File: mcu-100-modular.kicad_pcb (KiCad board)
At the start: 2 copper layers, 0 parts

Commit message: feat(mcu-100): actualizar esquematico, pcb y configuracion modular de espadines
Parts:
- added J1: Espadines_2x15_Macho, LUISMATERIALES:PinHeader_2x15_P2.54mm_Vertical, F.Cu at (140.6, 61.7)
- added J2: Espadines_2x15_Macho, LUISMATERIALES:PinHeader_2x15_P2.54mm_Vertical, F.Cu at (95.4, 57.0)
- added J3: Espadines_2x15_Macho, LUISMATERIALES:PinHeader_2x15_P2.54mm_Vertical, F.Cu at (131.5, 102.1)
- added J4: Espadines_2x15_Macho, LUISMATERIALES:PinHeader_2x15_P2.54mm_Vertical, F.Cu at (80.8, 61.8)
- added M1: Module-mcu-0.7, hellen-one-mcu-0.7:mcu, F.Cu at (88.8, 98.0)
- added M2: Module-mega-mcu144-0.7, hellen-one-mega-mcu144-0.7:mega-mcu144, F.Cu at (19.1, 73.7)
- added M4: Module:mega-mcu100/0.3, hellen-one-mega-mcu100-0.3:mega-mcu100, F.Cu at (36.3, 121.5)
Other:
- board outline added: 229.8 x 110 mm

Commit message: fix(bom): remover modulos extra M2 y M4 para eliminar duplicados de U105 en BOM
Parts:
- removed M2: Module-mega-mcu144-0.7, hellen-one-mega-mcu144-0.7:mega-mcu144
- removed M4: Module:mega-mcu100/0.3, hellen-one-mega-mcu100-0.3:mega-mcu100

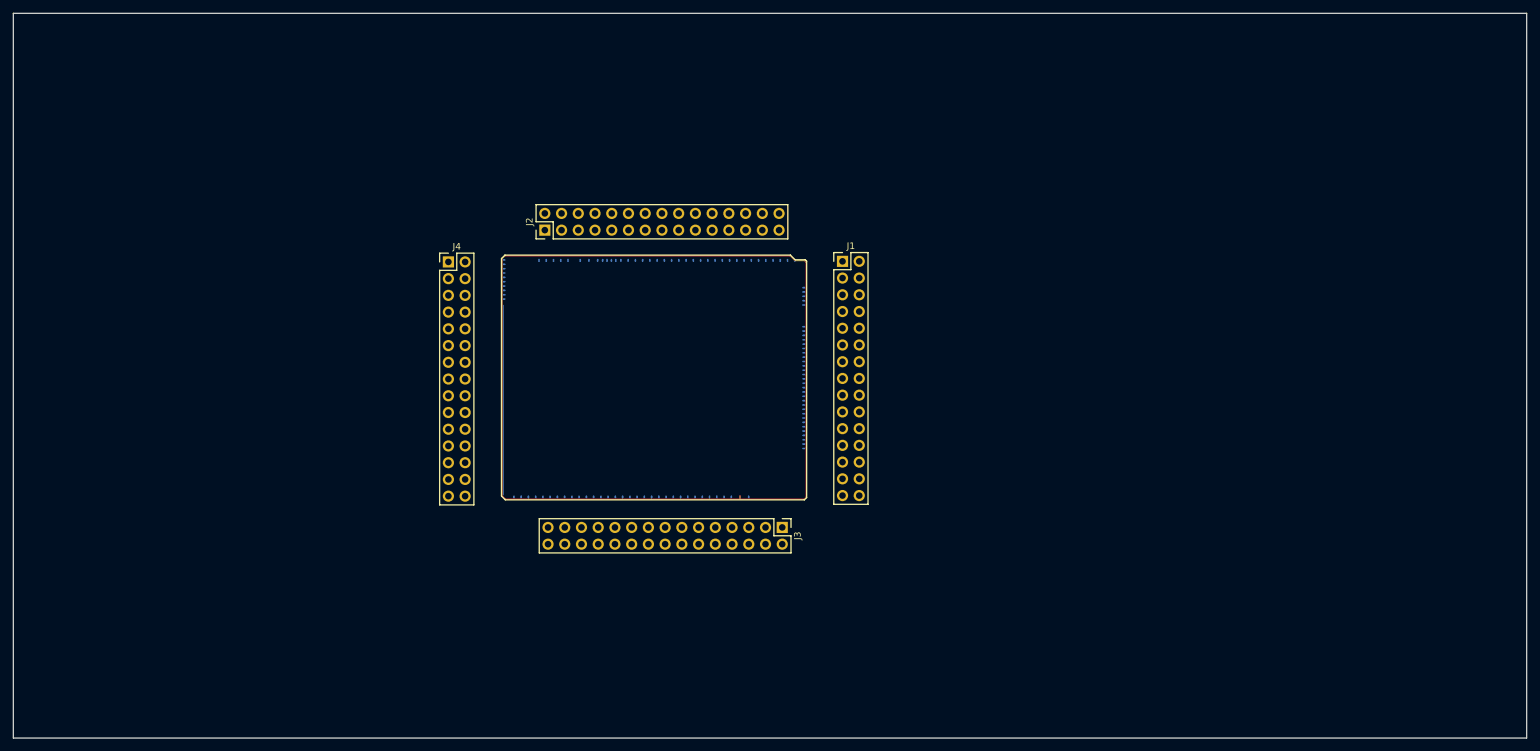
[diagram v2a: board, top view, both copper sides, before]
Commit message: feat(pcb, bom): actualizar sincronizacion PCB y anadir reemplazo U103 por AP2331SA-7 (C500764)
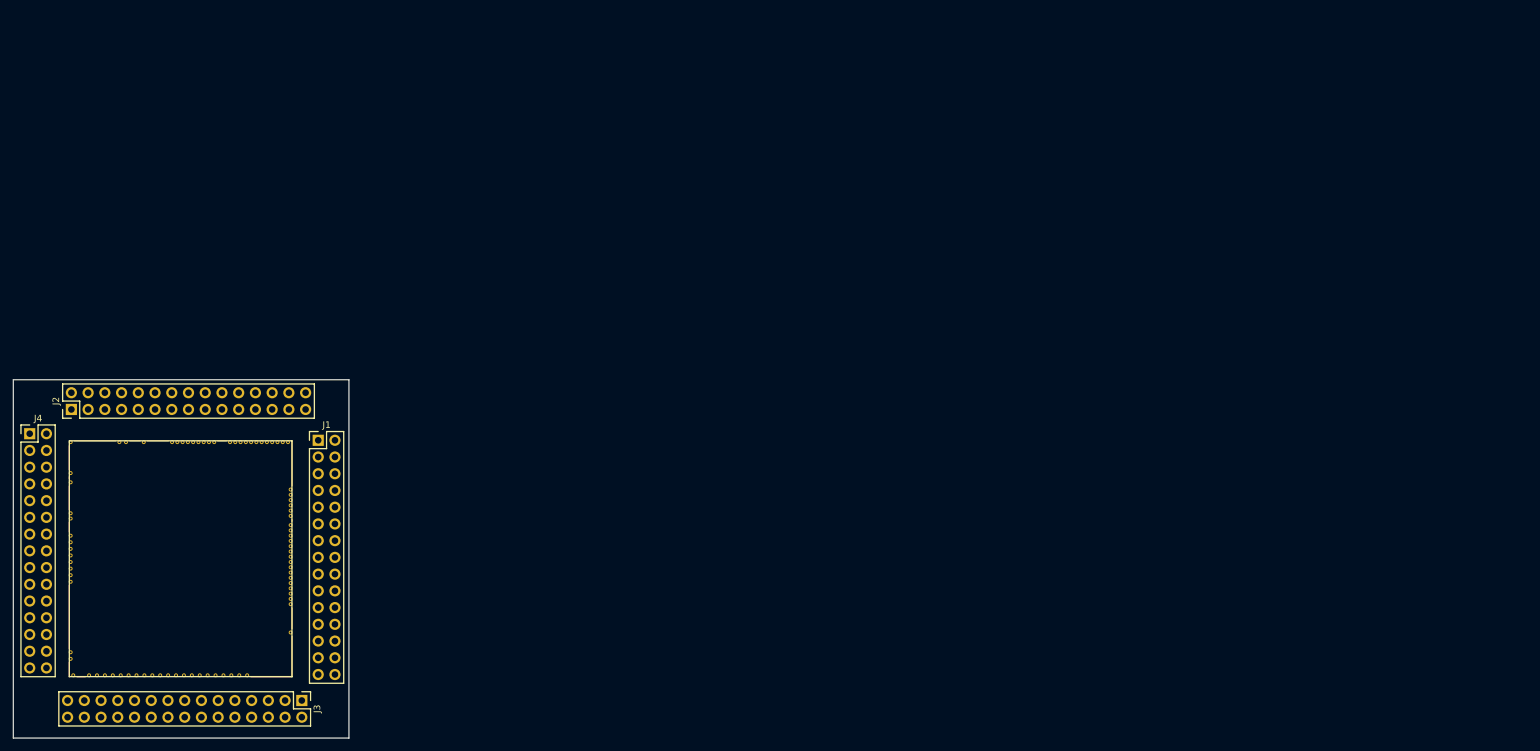
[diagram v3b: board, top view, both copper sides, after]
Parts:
- M1: value Module-mcu-0.7 -> Module:mega-mcu100/0.3; footprint hellen-one-mcu-0.7:mcu -> hellen-one-mega-mcu100-0.3:mega-mcu100
- moved J1 84.1 mm to (61.0, 88.9)
- moved J3 77.5 mm to (58.5, 128.4)
- moved J2 76.9 mm to (23.6, 84.2)
- moved M1 70.9 mm to (23.1, 124.9)
- moved J4 68.7 mm to (17.2, 87.9)
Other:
- board size 229.8 x 110 mm -> 51 x 54.4 mm

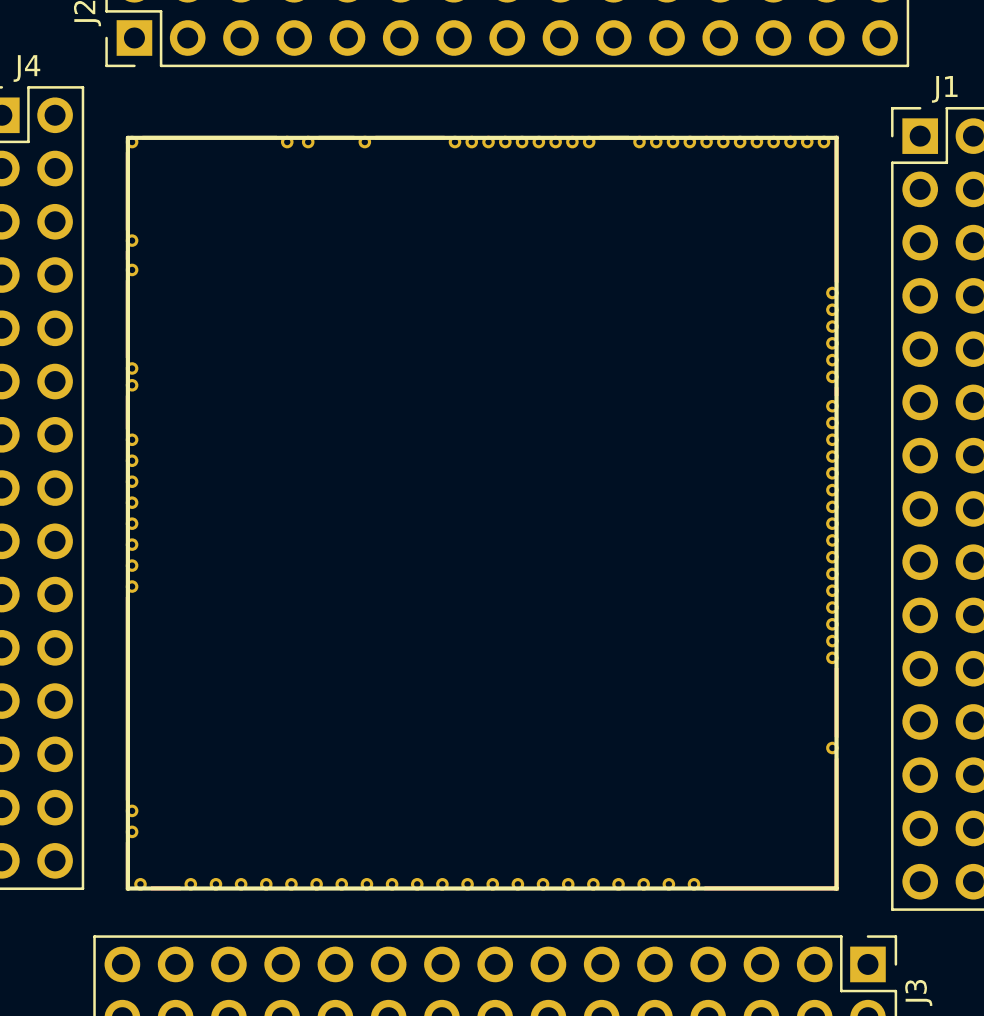
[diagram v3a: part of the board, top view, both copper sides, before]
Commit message: feat(sch, pcb): actualizar modulo M1 a mega-mcu100-0.3 y ajustar posicion en PCB
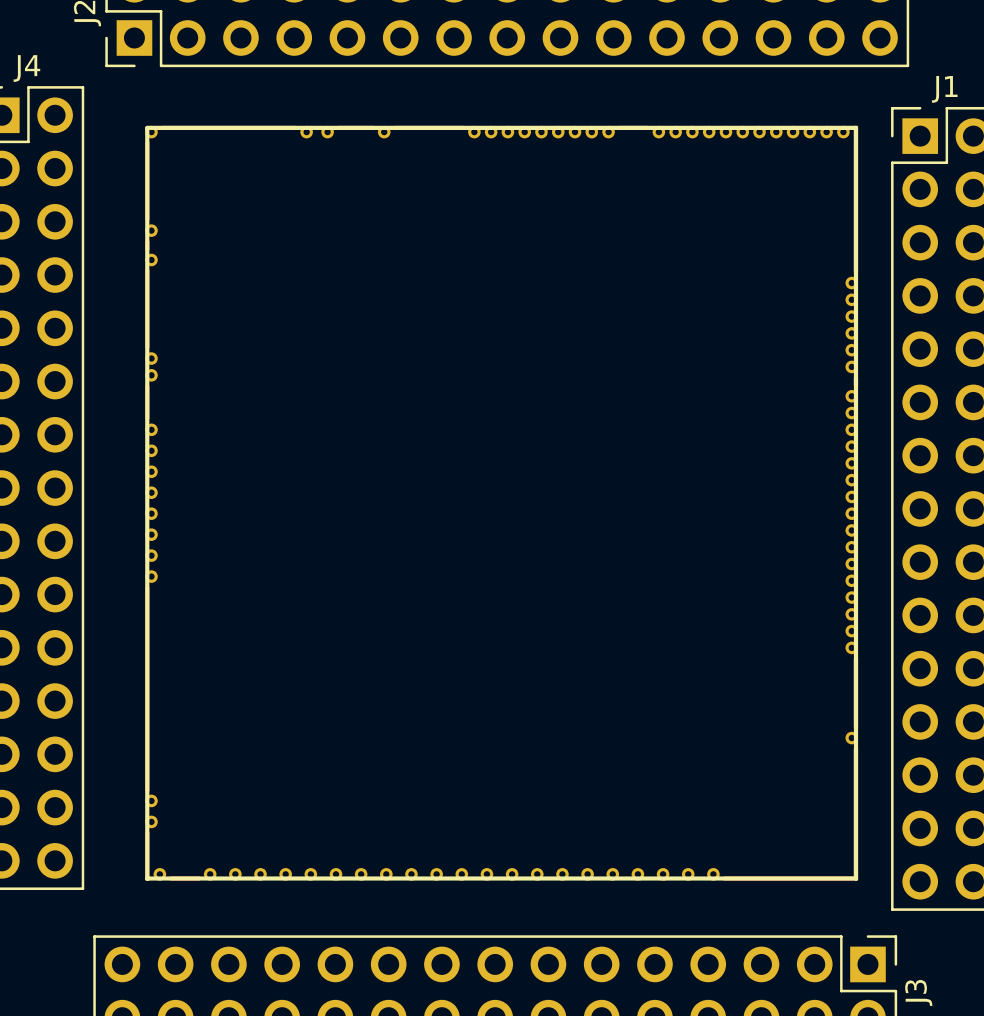
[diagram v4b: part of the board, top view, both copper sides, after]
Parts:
- moved M1 1.04 mm to (24.1, 124.4)
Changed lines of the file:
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@@
 	(footprint "hellen-one-mega-mcu100-0.3:mega-mcu100"
 		(layer "F.Cu")
-		(at 23.149995 124.875005)
+		(at 24.074995 124.400005)
 		(property "Reference" "M1"
 			(at 15.9258 -36.5252 0)
@@
 			(polygon
 				(pts
-					(xy 23.249995 88.975005) (xy 57.049995 88.975005) (xy 57.049995 124.775005) (xy 23.249995 124.775005)
+					(xy 24.174995 88.500005) (xy 57.974995 88.500005) (xy 57.974995 124.300005) (xy 24.174995 124.300005)
 				)
 			)
